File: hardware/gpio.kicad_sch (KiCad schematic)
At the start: 0 parts

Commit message: Initial layout
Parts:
- added J8: Conn_02x20_Odd_Even, Connector_PinHeader_2.54mm:PinHeader_2x20_P2.54mm_Vertical, symbol Connector_Generic:Conn_02x20_Odd_Even
- added J9: Conn_01x03, Connector_PinHeader_2.54mm:PinHeader_1x03_P2.54mm_Vertical, symbol Connector_Generic:Conn_01x03
- added Q2: BSN20, Package_TO_SOT_SMD:SOT-23, symbol Transistor_FET:BSN20
- added R35, R36: 33, Resistor_SMD:R_0402_1005Metric, symbol Device:R
- added R37: 10k, Resistor_SMD:R_0402_1005Metric, symbol Device:R
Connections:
- new net: Q2.2 (S), R35.2, R37.2
- new net: J9.1 (Pin_1), Q2.3 (D)
- new net: J9.2 (Pin_2), R36.2
- new net +3V3: Q2.1 (G), R37.1
- new net CPU_RX: R35.1
- new net CPU_TX: R36.1
- new net GND: J9.3 (Pin_3)
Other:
- note added: "TODO: LED"
- note added: "TVS omitted because well I'm on a budget..."

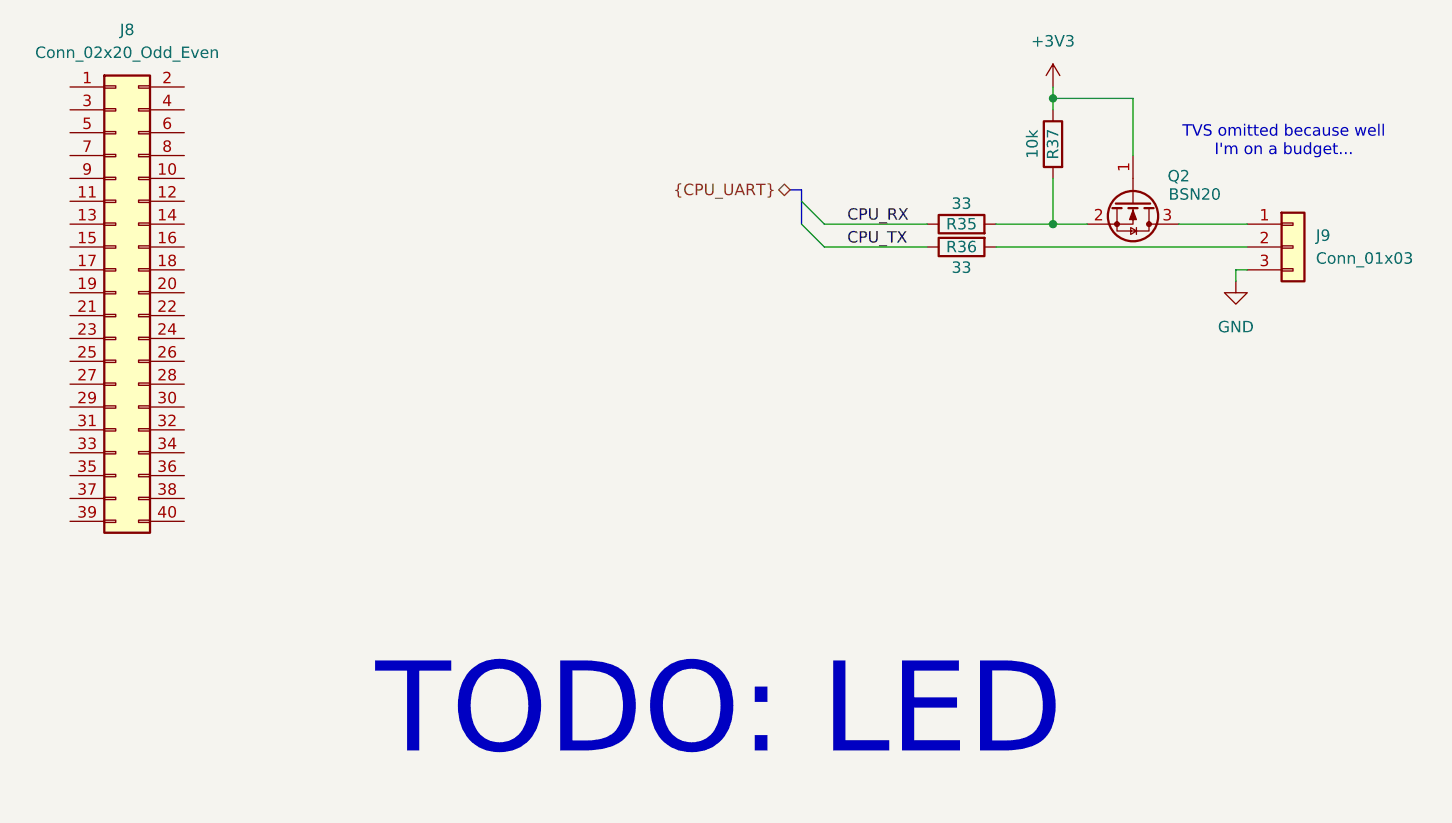
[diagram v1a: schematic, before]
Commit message: Finished DC DC converters and started decoupling the CPU
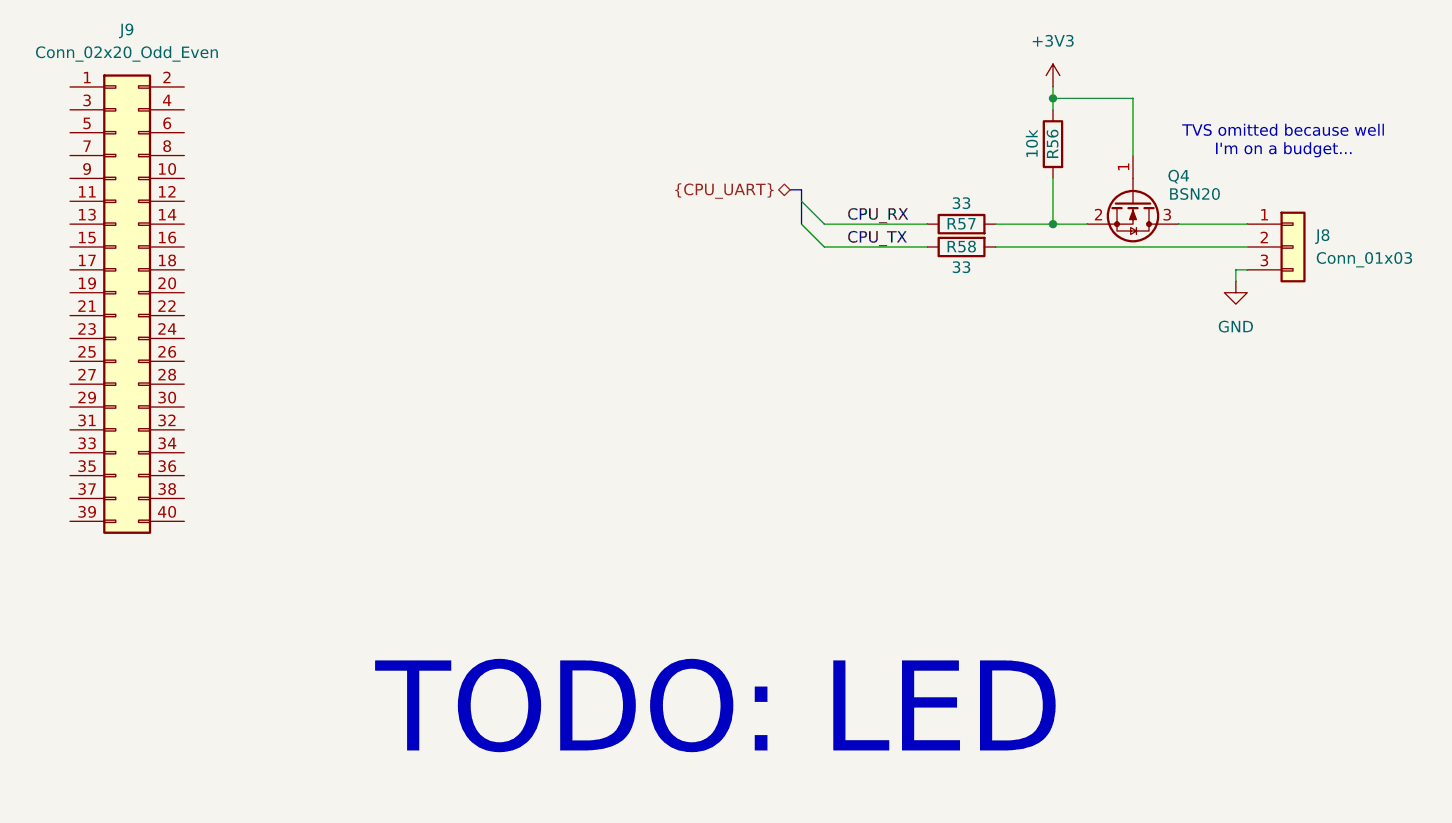
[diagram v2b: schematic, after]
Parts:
- renumbered J9 to J8, J8 to J9, Q2 to Q4, R37 to R56, R35 to R57, R36 to R58
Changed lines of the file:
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@@
 		(on_board yes)
 		(dnp no)
-		(property "Reference" "R37"
+		(property "Reference" "R56"
 			(at 177.8 92.71 90)
 			(effects
@@
 			(project "cm0"
 				(path "/b53f5dbb-8078-4818-9e8f-fdf90ba6d854/452e4208-fdd2-4279-8880-491fefaabe1c"
-					(reference "R37")
+					(reference "R56")
 					(unit 1)
 				)
@@
 		(on_board yes)
 		(dnp no)
-		(property "Reference" "R35"
+		(property "Reference" "R57"
 			(at 167.64 101.6 90)
 			(effects
@@
 			(project "cm0"
 				(path "/b53f5dbb-8078-4818-9e8f-fdf90ba6d854/452e4208-fdd2-4279-8880-491fefaabe1c"
-					(reference "R35")
+					(reference "R57")
 					(unit 1)
 				)
@@
 		(on_board yes)
 		(dnp no)
-		(property "Reference" "Q2"
+		(property "Reference" "Q4"
 			(at 191.77 96.266 90)
 			(effects
@@
 			(project "cm0"
 				(path "/b53f5dbb-8078-4818-9e8f-fdf90ba6d854/452e4208-fdd2-4279-8880-491fefaabe1c"
-					(reference "Q2")
+					(reference "Q4")
 					(unit 1)
 				)
@@
 		(dnp no)
 		(fields_autoplaced yes)
-		(property "Reference" "#PWR077"
+		(property "Reference" "#PWR0155"
 			(at 198.12 114.3 0)
 			(effects
@@
 			(project ""
 				(path "/b53f5dbb-8078-4818-9e8f-fdf90ba6d854/452e4208-fdd2-4279-8880-491fefaabe1c"
-					(reference "#PWR077")
+					(reference "#PWR0155")
 					(unit 1)
 				)
@@
 		(dnp no)
 		(fields_autoplaced yes)
-		(property "Reference" "#PWR076"
+		(property "Reference" "#PWR0154"
 			(at 177.8 90.17 0)
 			(effects
@@
 			(project ""
 				(path "/b53f5dbb-8078-4818-9e8f-fdf90ba6d854/452e4208-fdd2-4279-8880-491fefaabe1c"
-					(reference "#PWR076")
+					(reference "#PWR0154")
 					(unit 1)
 				)
@@
 		(dnp no)
 		(fields_autoplaced yes)
-		(property "Reference" "J9"
+		(property "Reference" "J8"
 			(at 207.01 102.8699 0)
 			(effects
@@
 			(project ""
 				(path "/b53f5dbb-8078-4818-9e8f-fdf90ba6d854/452e4208-fdd2-4279-8880-491fefaabe1c"
-					(reference "J9")
+					(reference "J8")
 					(unit 1)
 				)
@@
 		(dnp no)
 		(fields_autoplaced yes)
-		(property "Reference" "J8"
+		(property "Reference" "J9"
 			(at 74.93 80.01 0)
 			(effects
@@
 			(project ""
 				(path "/b53f5dbb-8078-4818-9e8f-fdf90ba6d854/452e4208-fdd2-4279-8880-491fefaabe1c"
-					(reference "J8")
+					(reference "J9")
 					(unit 1)
 				)
@@
 		(on_board yes)
 		(dnp no)
-		(property "Reference" "R36"
+		(property "Reference" "R58"
 			(at 167.64 104.14 90)
 			(effects
@@
 			(project "cm0"
 				(path "/b53f5dbb-8078-4818-9e8f-fdf90ba6d854/452e4208-fdd2-4279-8880-491fefaabe1c"
-					(reference "R36")
-					(unit 1)
-				)
+					(reference "R58")
+					(unit 1)
+				)

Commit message: Decoupling on PCB side almost done
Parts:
- J8, J9: now not fitted
- R57, R58: LCSC Part # (none) -> C25105
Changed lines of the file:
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@@
+			)
+		)
+		(property "FT Position Offset" ""
+			(at 177.8 92.71 90)
+			(effects
+				(font
+					(size 1.27 1.27)
+				)
+				(hide yes)
+			)
+		)
+		(property "FT Rotation Offset" ""
+			(at 177.8 92.71 90)
+			(effects
+				(font
+					(size 1.27 1.27)
+				)
+				(hide yes)
 			)
 		)
@@
 			)
 		)
-		(property "LCSC Part #" ""
+		(property "LCSC Part #" "C25105"
+			(at 167.64 101.6 90)
+			(effects
+				(font
+					(size 1.27 1.27)
+				)
+				(hide yes)
+			)
+		)
+		(property "FT Position Offset" ""
+			(at 167.64 101.6 90)
+			(effects
+				(font
+					(size 1.27 1.27)
+				)
+				(hide yes)
+			)
+		)
+		(property "FT Rotation Offset" ""
 			(at 167.64 101.6 90)
 			(effects
@@
 		)
 		(property "LCSC Part #" "C116157"
+			(at 186.69 99.06 90)
+			(effects
+				(font
+					(size 1.27 1.27)
+				)
+				(hide yes)
+			)
+		)
+		(property "FT Position Offset" ""
+			(at 186.69 99.06 90)
+			(effects
+				(font
+					(size 1.27 1.27)
+				)
+				(hide yes)
+			)
+		)
+		(property "FT Rotation Offset" ""
 			(at 186.69 99.06 90)
 			(effects
@@
 		(in_bom no)
 		(on_board yes)
-		(dnp no)
+		(dnp yes)
 		(fields_autoplaced yes)
 		(property "Reference" "J8"
@@
 		)
 		(property "Description" "Generic connector, single row, 01x03, script generated (kicad-library-utils/schlib/autogen/connector/)"
+			(at 204.47 104.14 0)
+			(effects
+				(font
+					(size 1.27 1.27)
+				)
+				(hide yes)
+			)
+		)
+		(property "FT Position Offset" ""
+			(at 204.47 104.14 0)
+			(effects
+				(font
+					(size 1.27 1.27)
+				)
+				(hide yes)
+			)
+		)
+		(property "FT Rotation Offset" ""
 			(at 204.47 104.14 0)
 			(effects
@@
 		(in_bom no)
 		(on_board yes)
-		(dnp no)
+		(dnp yes)
 		(fields_autoplaced yes)
 		(property "Reference" "J9"
@@
 		)
 		(property "Description" "Generic connector, double row, 02x20, odd/even pin numbering scheme (row 1 odd numbers, row 2 even numbers), script generated (kicad-library-utils/schlib/autogen/connector/)"
+			(at 73.66 109.22 0)
+			(effects
+				(font
+					(size 1.27 1.27)
+				)
+				(hide yes)
+			)
+		)
+		(property "FT Position Offset" ""
+			(at 73.66 109.22 0)
+			(effects
+				(font
+					(size 1.27 1.27)
+				)
+				(hide yes)
+			)
+		)
+		(property "FT Rotation Offset" ""
 			(at 73.66 109.22 0)
 			(effects
@@
 			)
 		)
-		(property "LCSC Part #" ""
+		(property "LCSC Part #" "C25105"
 			(at 167.64 104.14 90)
 			(effects
+				(font
+					(size 1.27 1.27)
+				)
+				(hide yes)
+			)
+		)
+		(property "FT Position Offset" ""
+			(at 167.64 104.14 90)
+			(effects
+				(font
+					(size 1.27 1.27)
+				)
+				(hide yes)
+			)
+		)
+		(property "FT Rotation Offset" ""
+			(at 167.64 104.14 90)
+			(effects

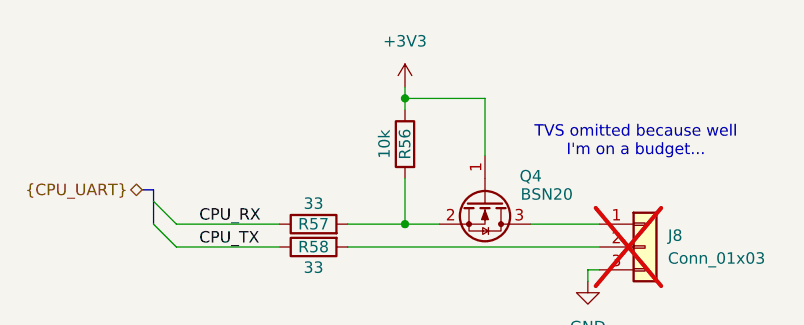
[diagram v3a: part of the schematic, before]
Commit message: Routed DCDC, EPHY and SD
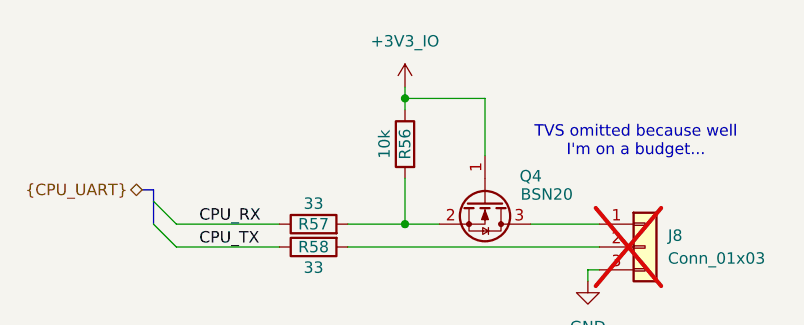
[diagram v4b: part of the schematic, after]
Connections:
- net +3V3 renamed +3V3_IO
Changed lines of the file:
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@@
+	)
+	(symbol
+		(lib_id "cm0:+3V3_IO")
+		(at 177.8 86.36 0)
+		(unit 1)
+		(exclude_from_sim no)
+		(in_bom yes)
+		(on_board yes)
+		(dnp no)
+		(fields_autoplaced yes)
+		(property "Reference" "#PWR0154"
+			(at 177.8 90.17 0)
+			(effects
+				(font
+					(size 1.27 1.27)
+				)
+				(hide yes)
+			)
+		)
+		(property "Value" "+3V3_IO"
+			(at 177.8 81.28 0)
+			(effects
+				(font
+					(size 1.27 1.27)
+				)
+			)
+		)
+		(property "Footprint" ""
+			(at 177.8 86.36 0)
+			(effects
+				(font
+					(size 1.27 1.27)
+				)
+				(hide yes)
+			)
+		)
+		(property "Datasheet" ""
+			(at 177.8 86.36 0)
+			(effects
+				(font
+					(size 1.27 1.27)
+				)
+				(hide yes)
+			)
+		)
+		(property "Description" "Power symbol creates a global label with name \"+3V3_IO\""
+			(at 177.8 86.36 0)
+			(effects
+				(font
+					(size 1.27 1.27)
+				)
+				(hide yes)
+			)
+		)
+		(pin "1"
+		)
+		(instances
+			(project ""
+				(path "/b53f5dbb-8078-4818-9e8f-fdf90ba6d854/452e4208-fdd2-4279-8880-491fefaabe1c"
+					(reference "#PWR0154")
+					(unit 1)
+				)
+			)
+		)
 	)
 	(symbol
@@
 					(unit 1)
 				)
-			)
-		)
-	)
-	(symbol
-		(lib_id "power:+3V3")
-		(at 177.8 86.36 0)
-		(unit 1)
-		(exclude_from_sim no)
-		(in_bom yes)
-		(on_board yes)
-		(dnp no)
-		(fields_autoplaced yes)
-		(property "Reference" "#PWR0154"
-			(at 177.8 90.17 0)
-			(effects
-				(font
-					(size 1.27 1.27)
-				)
-				(hide yes)
-			)
-		)
-		(property "Value" "+3V3"
-			(at 177.8 81.28 0)
-			(effects
-				(font
-					(size 1.27 1.27)
-				)
-			)
-		)
-		(property "Footprint" ""
-			(at 177.8 86.36 0)
-			(effects
-				(font
-					(size 1.27 1.27)
-				)
-				(hide yes)
-			)
-		)
-		(property "Datasheet" ""
-			(at 177.8 86.36 0)
-			(effects
-				(font
-					(size 1.27 1.27)
-				)
-				(hide yes)
-			)
-		)
-		(property "Description" "Power symbol creates a global label with name \"+3V3\""
-			(at 177.8 86.36 0)
-			(effects
-				(font
-					(size 1.27 1.27)
-				)
-				(hide yes)
-			)
-		)
-		(pin "1"
-		)
-		(instances
-			(project ""
-				(path "/b53f5dbb-8078-4818-9e8f-fdf90ba6d854/452e4208-fdd2-4279-8880-491fefaabe1c"
-					(reference "#PWR0154")
-					(unit 1)
-				)
